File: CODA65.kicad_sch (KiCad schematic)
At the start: 28 parts, among them J1 Conn_01x04, J2 Conn_01x05, SW1 SW_Push, SW2 SW_Push, U1 RP2040, U2 W25Q128JVS, U4 XC6206PxxxMR, Y1 Crystal_GND24

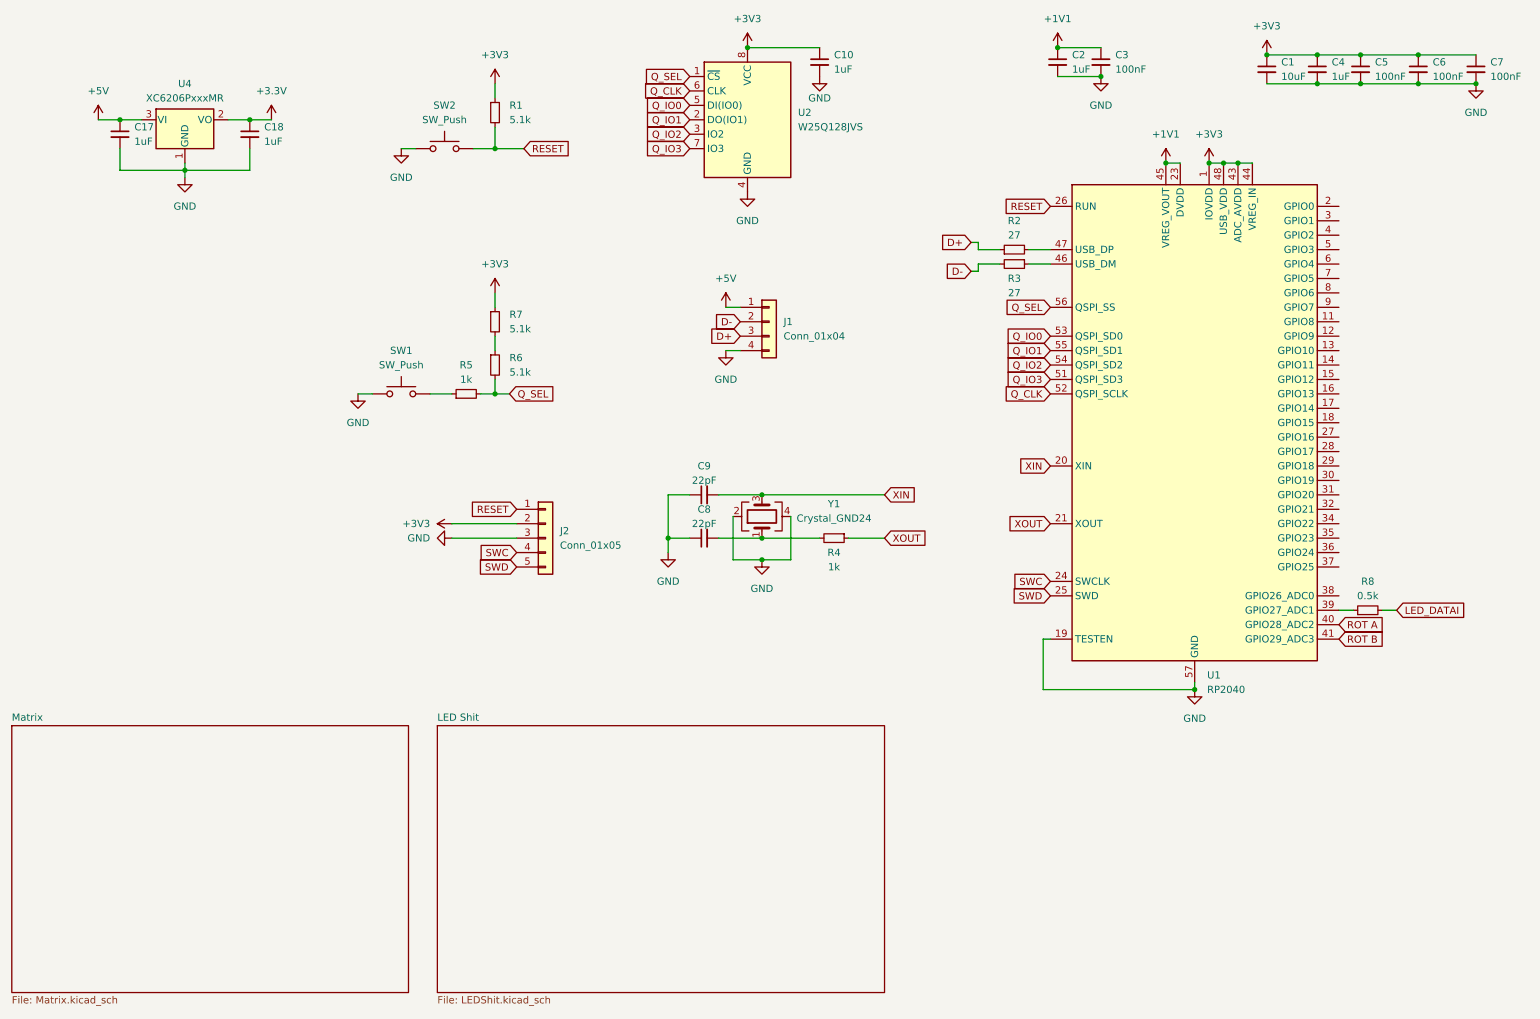
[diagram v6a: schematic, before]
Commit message: Fixes and routing
Routed Col and Row for switches.
Fixed annotation of LEDs and caps.
Started LED matrix Routing.
Started mcu and supporting routing.
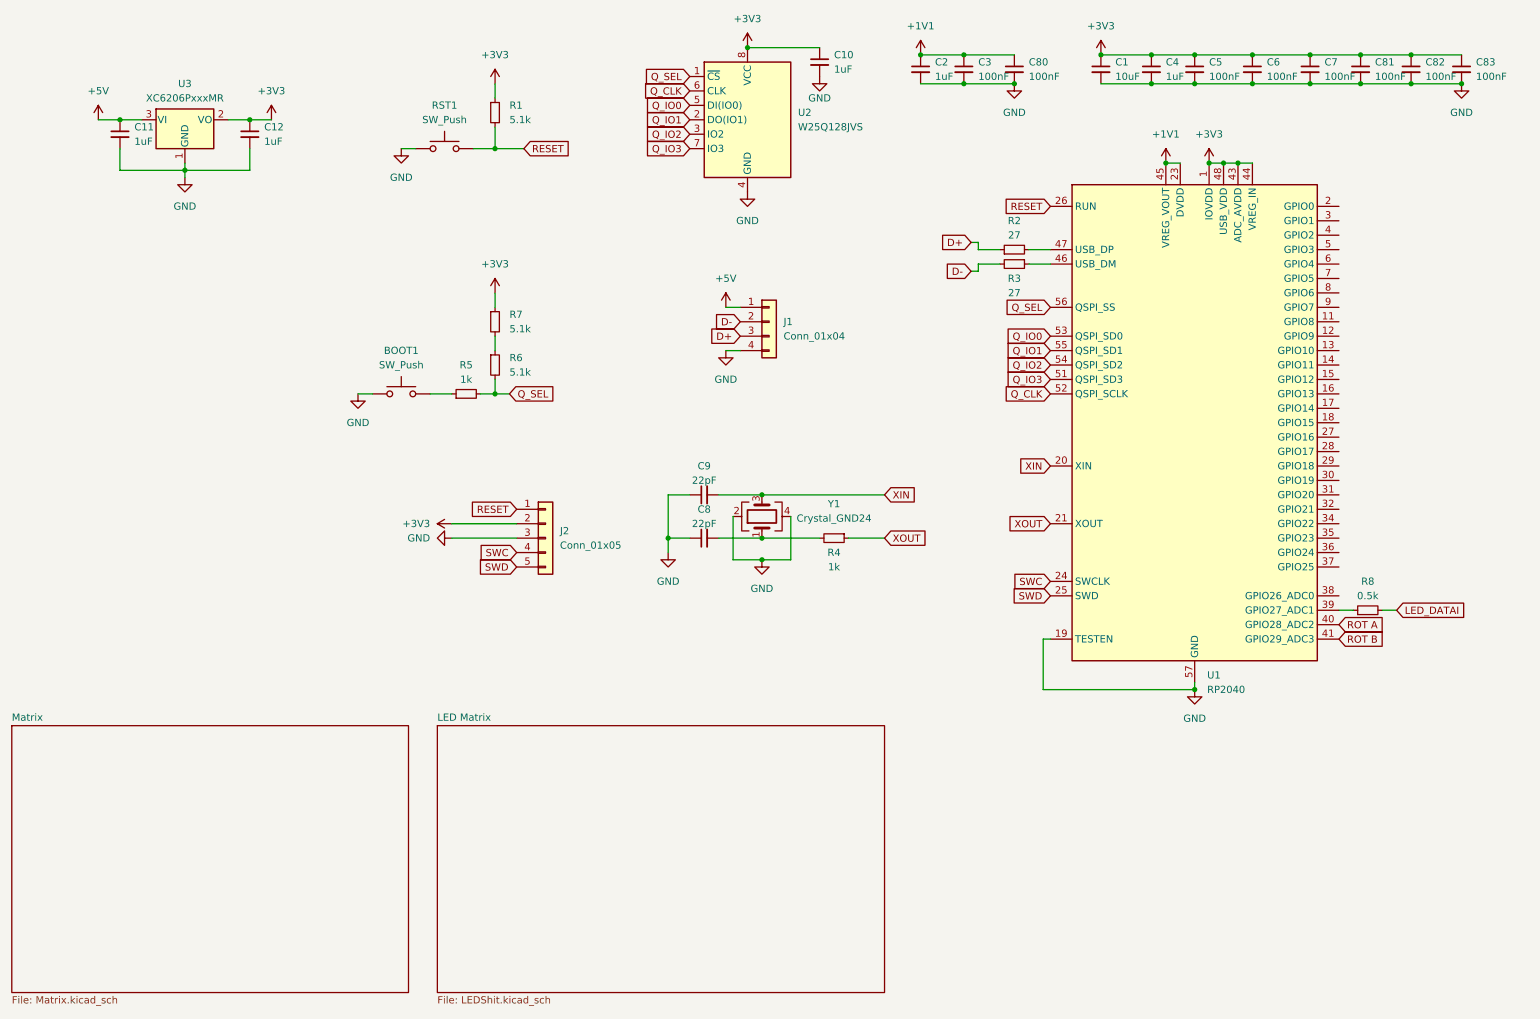
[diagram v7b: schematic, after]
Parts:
- added C80, C81, C82, C83: 100nF, Capacitor_SMD:C_0402_1005Metric, symbol Device:C_Small
- renumbered SW1 to BOOT1, C17 to C11, C18 to C12, SW2 to RST1, U4 to U3
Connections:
- net +3.3V is gone; now on net +3V3: C12.1, U3.2 (VO)
- net +1V1: now also C80.1
- net +3V3: now also C81.1, C82.1, C83.1
- net GND: now also C80.2, C81.2, C82.2, C83.2
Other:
- sheet LED Shit renamed LED Matrix
- moved on the sheet: C1, C2, C3, C4, C5, C6, C7

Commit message: Routed more of matrix; Grounded
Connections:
- net +3V3: now also J2.4 (Pin_4); no longer J2.2 (Pin_2)
- net GND: now also J2.5 (Pin_5); no longer J2.3 (Pin_3)
- net RESET: now also J2.3 (Pin_3); no longer J2.1 (Pin_1)
- net SWC: now also J2.1 (Pin_1); no longer J2.4 (Pin_4)
- net SWD: now also J2.2 (Pin_2); no longer J2.5 (Pin_5)
- net COL10: now reaches U1.16 (GPIO13)
- net COL11: now reaches U1.17 (GPIO14)
- net COL13: now reaches U1.18 (GPIO15)
- net COL4: now reaches U1.2 (GPIO0)
- net COL5: now reaches U1.3 (GPIO1)
- net COL3: now reaches U1.35 (GPIO23)
- net COL2: now reaches U1.36 (GPIO24)
- net COL1: now reaches U1.37 (GPIO25)
- net Col0: now reaches U1.38 (GPIO26_ADC0)
- net COL7: now reaches U1.4 (GPIO2)
- net COL8: now reaches U1.5 (GPIO3)
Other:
- moved on the sheet: R8
